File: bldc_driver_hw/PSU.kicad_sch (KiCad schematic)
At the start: 0 parts

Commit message: wip
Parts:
- added C1, C11, C16, C2, C3, C9: 100nF, Capacitor_SMD:C_0603_1608Metric_Pad1.08x0.95mm_HandSolder, symbol Device:C_Small
- added C10, C8: 47uF, Capacitor_SMD:C_0603_1608Metric_Pad1.08x0.95mm_HandSolder, symbol Device:C_Small
- added C12, C13, C14, C15, C4, C5: 10uF, Capacitor_SMD:C_0805_2012Metric_Pad1.18x1.45mm_HandSolder, symbol Device:C_Small
- added C6: 6.8nF, Capacitor_SMD:C_0603_1608Metric_Pad1.08x0.95mm_HandSolder, symbol Device:C_Small
- added C7: 6.8pF, Capacitor_SMD:C_0603_1608Metric_Pad1.08x0.95mm_HandSolder, symbol Device:C_Small
- added D1: 100V / 4A, Diode_SMD:D_SMB_Handsoldering, symbol Device:D_Schottky
- added L1: 68uH, symbol Device:L
- added R1: 140k, Resistor_SMD:R_0603_1608Metric_Pad0.98x0.95mm_HandSolder, symbol Device:R_Small
- added R2: 10k, Resistor_SMD:R_0603_1608Metric_Pad0.98x0.95mm_HandSolder, symbol Device:R_Small
- added R5: 100k, Resistor_SMD:R_0603_1608Metric_Pad0.98x0.95mm_HandSolder, symbol Device:R_Small
- added R6: 680k, Resistor_SMD:R_0603_1608Metric_Pad0.98x0.95mm_HandSolder, symbol Device:R_Small
- added U1: AMS1117-3.3, Package_TO_SOT_SMD:SOT-223-3_TabPin2, symbol Regulator_Linear:AMS1117-3.3
- added U2: TPS54260DGQ, Package_SO:MSOP-10-1EP_3x3mm_P0.5mm_EP2.2x3.1mm_Mask1.83x1.89mm_ThermalVias, symbol Regulator_Switching:TPS54260DGQ
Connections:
- new net: C7.1, R5.1, U2.8 (COMP)
- new net: R1.2, R2.1, U2.7 (VSENSE)
- new net: C1.2, D1.1 (K), L1.1, U2.1 (BOOT)
- new net: C1.1, U2.10 (PH)
- new net: C6.1, U2.4 (SS/TR)
- new net: R6.1, U2.5 (RT/CLK)
- new net: C3.1, R5.2
- new net +3.3V: C11.1, C14.1, C15.1, U1.2 (VO)
- new net +48V: C2.1, C4.1, C5.1, U2.2 (VIN)
- new net +5V: C12.1, C13.1, C16.1, U1.3 (VI)
- new net GND: C10.2, C11.2, C12.2, C13.2, C14.2, C15.2, C16.2, C2.2, C3.2, C4.2, C5.2, C6.2, C7.2, C8.2, C9.2, D1.2 (A), R2.2, R6.2, U1.1 (GND), U2.11 (GND), U2.9 (GND)
- new net Vdrive: C10.1, C8.1, C9.1, L1.2, R1.1
- no-connect marks 0 -> 2

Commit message: wip
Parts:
- added D7, D8: SS24, Diode_SMD:D_SMA, symbol Diode:SS24
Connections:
- net +5V: now also D7.1 (K), D8.1 (K)
- new net +5VD: D8.2 (A)
- new net VBUS: D7.2 (A)
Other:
- note added: "12V Aktualnie"
- moved on the sheet: C11, C12, C13, C14, C15, C16, R1, R2, U1

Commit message: wip
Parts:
- added D10: SS24, Diode_SMD:D_SMA, symbol Diode:SS24
- added NMT: 100k, Resistor_SMD:R_0603_1608Metric_Pad0.98x0.95mm_HandSolder, symbol Device:R_Small
- added R36: NMT, Resistor_SMD:R_0603_1608Metric_Pad0.98x0.95mm_HandSolder, symbol Device:R_Small
- L1: value 68uH -> 33uH; footprint (none) -> Inductor_SMD:L_Vishay_IHLP-4040
- R1: value 140k -> 52.3k
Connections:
- net Vdrive is gone; now on net +5V: C10.1, C8.1, C9.1, L1.2, R1.1
- net +48V: now also R36.1
- net +5V: now also D10.1 (K)
- net GND: now also NMT.2
- net at U2.3 (EN): now also NMT.1, R36.2
- new net VBUS2: D10.2 (A)
- no-connect marks 2 -> 1
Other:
- note removed: "12V Aktualnie"
- moved on the sheet: C1, C10, C11, C12, C13, C14, C15, C16, C2, C3, C4, C5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

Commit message: schematic finished pcb in progress
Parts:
- added TP4, TP5, TP6, TP7, TP8, TP9: TestPoint, TestPoint:TestPoint_Pad_D2.0mm, symbol Connector:TestPoint
- R11: renamed from R36; footprint Resistor_SMD:R_0603_1608Metric_Pad0.98x0.95mm_HandSolder -> Resistor_SMD:R_0603_1608Metric
- renumbered C12 to C10, C16 to C11, C1 to C12, C14 to C13, C15 to C14, C11 to C15, C8 to C16, C10 to C17, C9 to C18, C4 to C3, C5 to C4, C2 to C5, C7 to C6, C3 to C7, C6 to C8, C13 to C9, D8 to D1, D7 to D2, D10 to D3, D1 to D4, NMT to NMT1, R5 to R12, R6 to R13, R1 to R14, R2 to R15, U2 to U3, U1 to U4
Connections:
- net +3.3V: now also TP9.1
- net +5V: now also TP7.1; no longer C16.1, C17.1, C18.1, L1.2, R14.1
- net +5VD: now also C16.1, C17.1, C18.1, L1.2, R14.1, TP4.1
- net VBUS: now also TP5.1
- net VBUS2: now also TP6.1
- net +48V renamed VDD
- net VDD: now also TP8.1
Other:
- moved on the sheet: C13, C3, C4, C5, C6, C7, C8, NMT1, R11, R12, R13

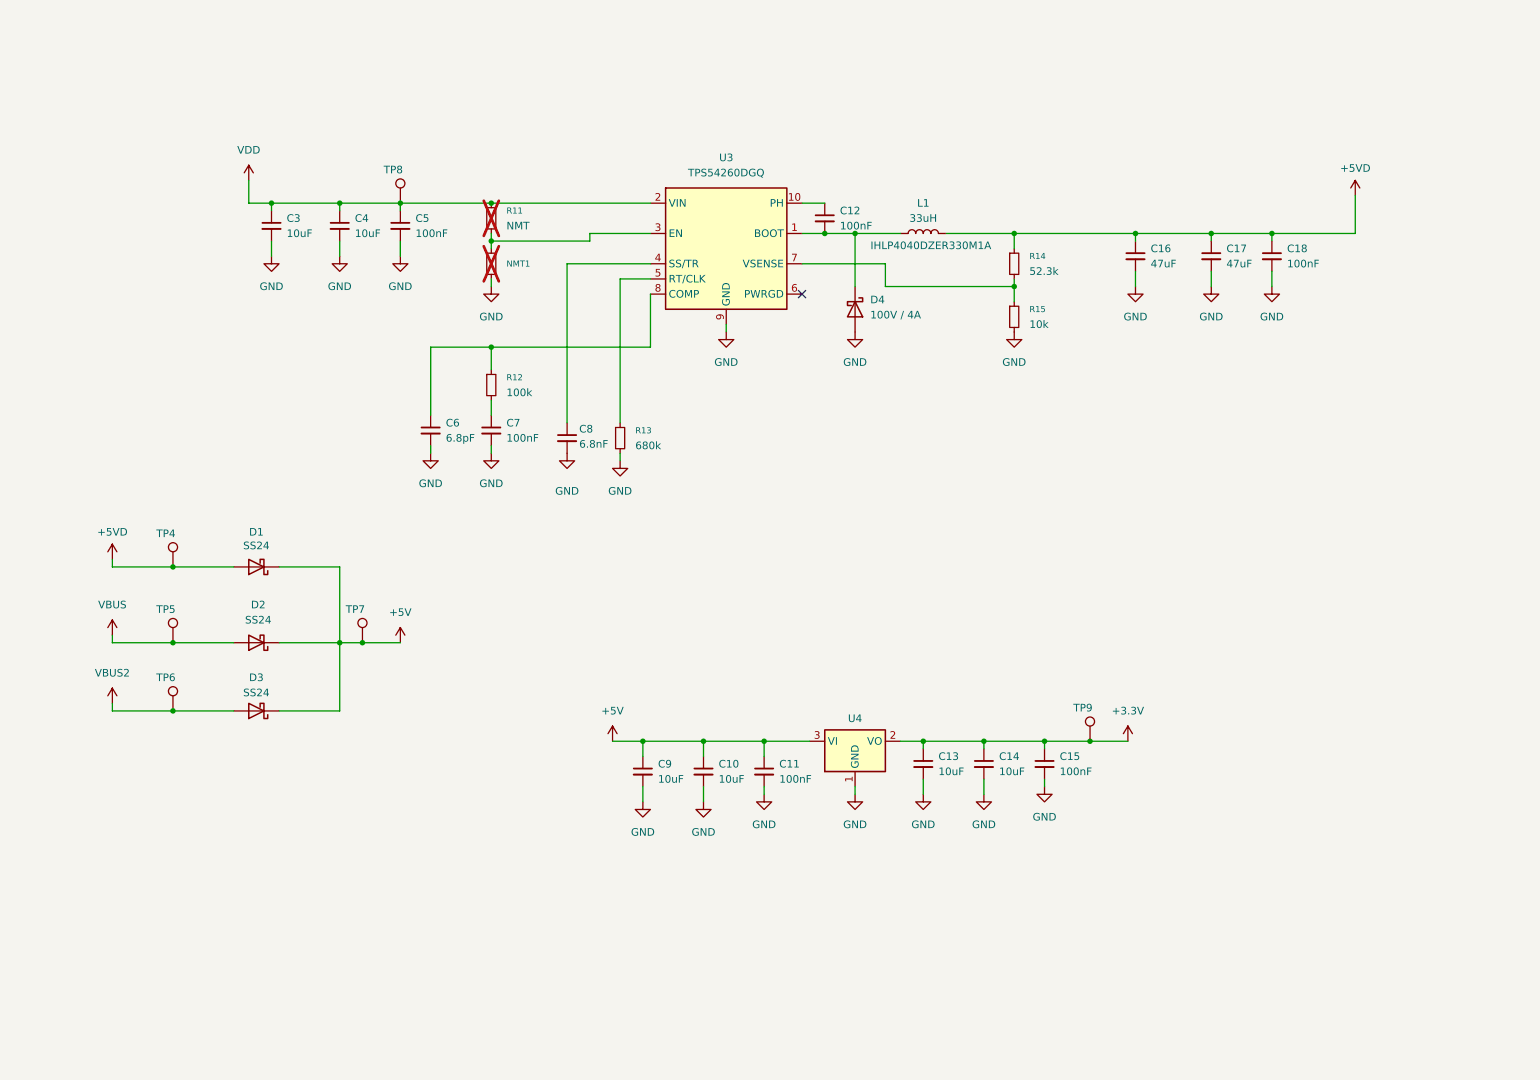
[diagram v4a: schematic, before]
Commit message: Changed one 3 phase driver to three h-bridges and changed buck converter which sink more current
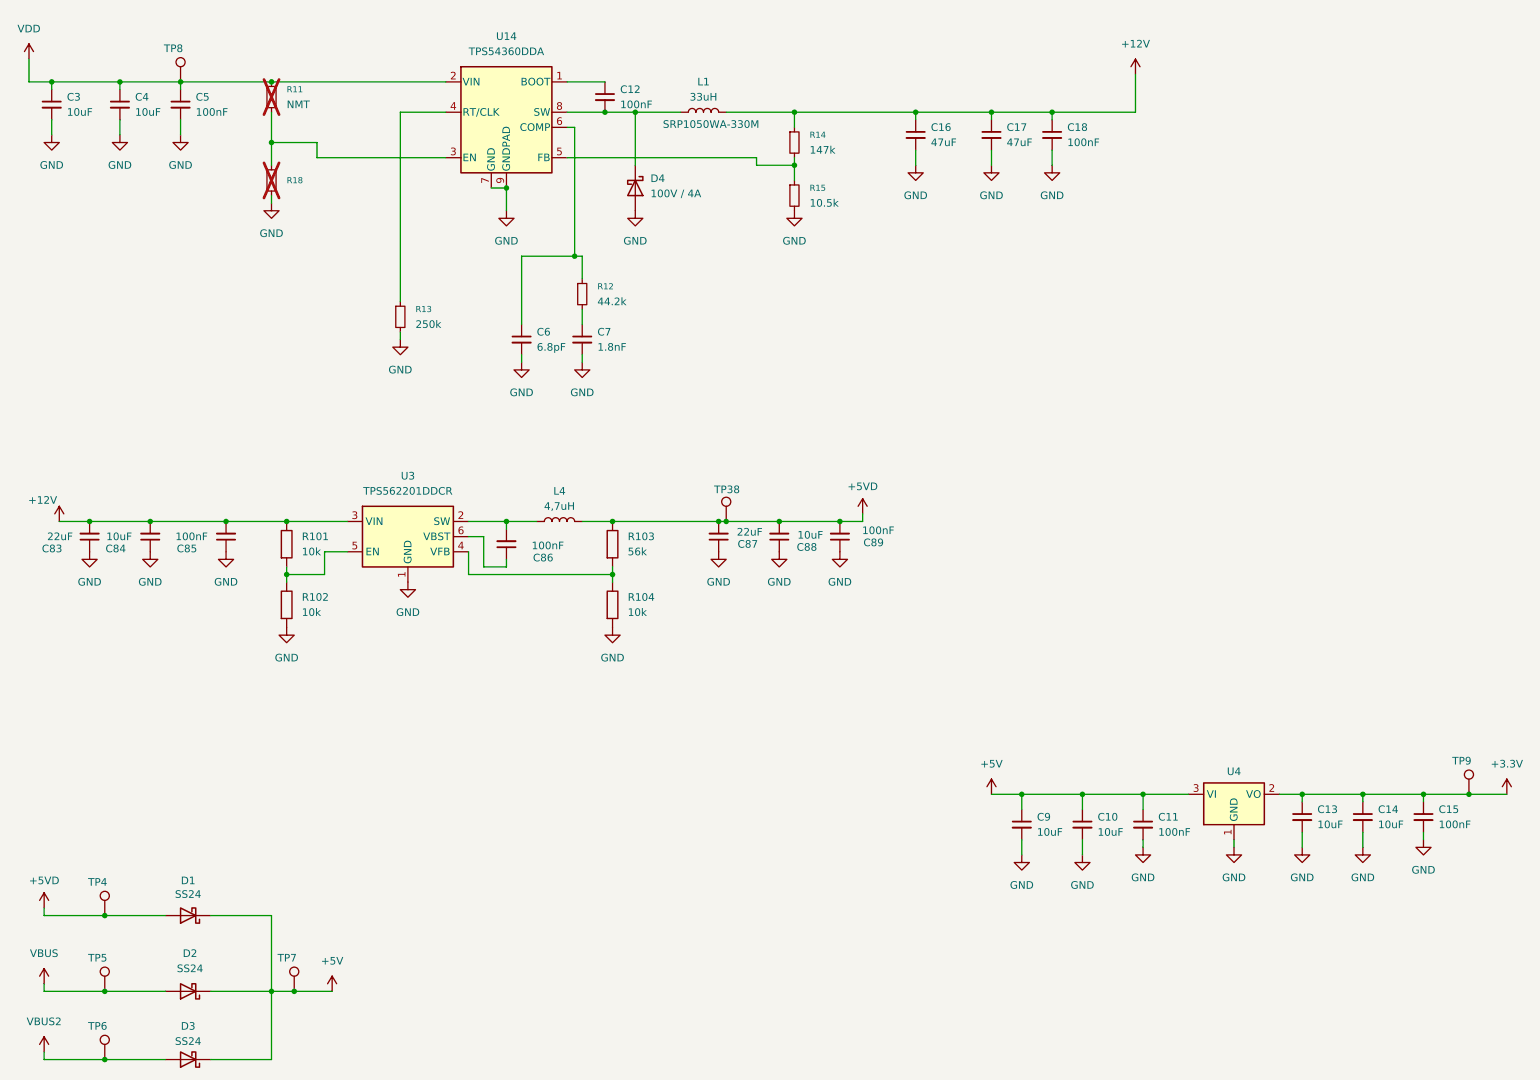
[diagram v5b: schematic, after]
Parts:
- removed C8: 6.8nF, Capacitor_SMD:C_0603_1608Metric_Pad1.08x0.95mm_HandSolder, symbol Device:C_Small
- removed U3: TPS54260DGQ, Package_SO:MSOP-10-1EP_3x3mm_P0.5mm_EP2.2x3.1mm_Mask1.83x1.89mm_ThermalVias, symbol Regulator_Switching:TPS54260DGQ
- added C83, C87: 22uF, Capacitor_SMD:C_0805_2012Metric_Pad1.18x1.45mm_HandSolder, symbol Device:C_Small
- added C84, C88: 10uF, Capacitor_SMD:C_0603_1608Metric_Pad1.08x0.95mm_HandSolder, symbol Device:C_Small
- added C85, C86, C89: 100nF, Capacitor_SMD:C_0603_1608Metric_Pad1.08x0.95mm_HandSolder, symbol Device:C_Small
- added L4: 4,7uH, bldc_driver_footprint:INDPM5452X300N, symbol Device:L
- added R101, R102, R104: 10k, Resistor_SMD:R_0603_1608Metric_Pad0.98x0.95mm_HandSolder, symbol PCM_SL_Resistors:Resistor
- added R103: 56k, Resistor_SMD:R_0603_1608Metric_Pad0.98x0.95mm_HandSolder, symbol PCM_SL_Resistors:Resistor
- added TP38: TestPoint, TestPoint:TestPoint_Pad_D2.0mm, symbol Connector:TestPoint
- added U14: TPS54360DDA, Package_SO:TI_SO-PowerPAD-8_ThermalVias, symbol Regulator_Switching:TPS54360DDA
- added U3: TPS562201DDCR, Package_TO_SOT_SMD:SOT-23-6_Handsoldering, symbol Regulator_Switching:TPS562200
- C7: value 100nF -> 1.8nF
- L1: footprint Inductor_SMD:L_Vishay_IHLP-4040 -> Inductor_SMD:L_Bourns_SRP1050WA
- R12: value 100k -> 44.2k
- R13: value 680k -> 250k
- R14: value 52.3k -> 147k; footprint Resistor_SMD:R_0603_1608Metric_Pad0.98x0.95mm_HandSolder -> Resistor_SMD:R_0603_1608Metric
- R15: value 10k -> 10.5k; footprint Resistor_SMD:R_0603_1608Metric_Pad0.98x0.95mm_HandSolder -> Resistor_SMD:R_0603_1608Metric
- R18: renamed from NMT1; footprint Resistor_SMD:R_0603_1608Metric_Pad0.98x0.95mm_HandSolder -> Resistor_SMD:R_0603_1608Metric
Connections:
- net +5VD: now also C87.2, C88.2, C89.2, L4.2, R103.2, TP38.1; no longer C16.1, C17.1, C18.1, L1.2, R14.1
- net GND: now also C83.1, C84.1, C85.1, C87.1, C88.1, C89.1, R102.1, R104.1, U14.7 (GND), U14.9 (GNDPAD), U3.1 (GND)
- net VDD: now also U14.2 (VIN)
- net at C6.1, R12.1: now also U14.6 (COMP)
- net at R14.2, R15.1: now also U14.5 (FB)
- net at C12.2, D4.1 (K), L1.1: now also U14.8 (SW)
- net at C12.1: now also U14.1 (BOOT)
- net at R11.2, R18.1: now also U14.3 (EN)
- net at R13.1: now also U14.4 (RT/CLK)
- new net: R103.1, R104.2, U3.4 (VFB)
- new net: R101.1, R102.2, U3.5 (EN)
- new net: C86.2, L4.1, U3.2 (SW)
- new net: C86.1, U3.6 (VBST)
- new net +12V: C16.1, C17.1, C18.1, C83.2, C84.2, C85.2, L1.2, R101.2, R14.1, U3.3 (VIN)
- no-connect marks 1 -> 0
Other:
- moved on the sheet: C10, C11, C12, C13, C14, C15, C16, C17, C18, C3, C4, C5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

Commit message: Board finished to review
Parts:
- removed TP4: TestPoint, TestPoint:TestPoint_Pad_D2.0mm, symbol Connector:TestPoint
- added TP15: TestPoint, TestPoint:TestPoint_Pad_D2.0mm, symbol Connector:TestPoint
- C10, C13, C14, C9: footprint Capacitor_SMD:C_0805_2012Metric_Pad1.18x1.45mm_HandSolder -> Capacitor_SMD:C_0603_1608Metric
- C11, C12, C15, C16, C17, C18, C5, C6, C7, C84, C85, C86, C88, C89: footprint Capacitor_SMD:C_0603_1608Metric_Pad1.08x0.95mm_HandSolder -> Capacitor_SMD:C_0603_1608Metric
- C3, C4, C83, C87: footprint Capacitor_SMD:C_0805_2012Metric_Pad1.18x1.45mm_HandSolder -> Capacitor_SMD:C_0805_2012Metric
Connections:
- net +12V: now also TP15.1

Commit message: wip
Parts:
- R101, R102, R103, R104, R12, R13: footprint Resistor_SMD:R_0603_1608Metric_Pad0.98x0.95mm_HandSolder -> Resistor_SMD:R_0603_1608Metric
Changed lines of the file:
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@@
 			)
 		)
-		(property "Footprint" "Resistor_SMD:R_0603_1608Metric_Pad0.98x0.95mm_HandSolder"
+		(property "Footprint" "Resistor_SMD:R_0603_1608Metric"
 			(at 81.28 66.04 0)
 			(effects
@@
 			)
 		)
-		(property "Footprint" "Resistor_SMD:R_0603_1608Metric_Pad0.98x0.95mm_HandSolder"
+		(property "Footprint" "Resistor_SMD:R_0603_1608Metric"
 			(at 121.158 113.411 0)
 			(effects
@@
 			)
 		)
-		(property "Footprint" "Resistor_SMD:R_0603_1608Metric_Pad0.98x0.95mm_HandSolder"
+		(property "Footprint" "Resistor_SMD:R_0603_1608Metric"
 			(at 66.548 113.411 0)
 			(effects
@@
 			)
 		)
-		(property "Footprint" "Resistor_SMD:R_0603_1608Metric_Pad0.98x0.95mm_HandSolder"
+		(property "Footprint" "Resistor_SMD:R_0603_1608Metric"
 			(at 111.76 62.23 0)
 			(effects
@@
 			)
 		)
-		(property "Footprint" "Resistor_SMD:R_0603_1608Metric_Pad0.98x0.95mm_HandSolder"
+		(property "Footprint" "Resistor_SMD:R_0603_1608Metric"
 			(at 121.158 103.251 0)
 			(effects
@@
 			)
 		)
-		(property "Footprint" "Resistor_SMD:R_0603_1608Metric_Pad0.98x0.95mm_HandSolder"
+		(property "Footprint" "Resistor_SMD:R_0603_1608Metric"
 			(at 66.548 103.251 0)
 			(effects

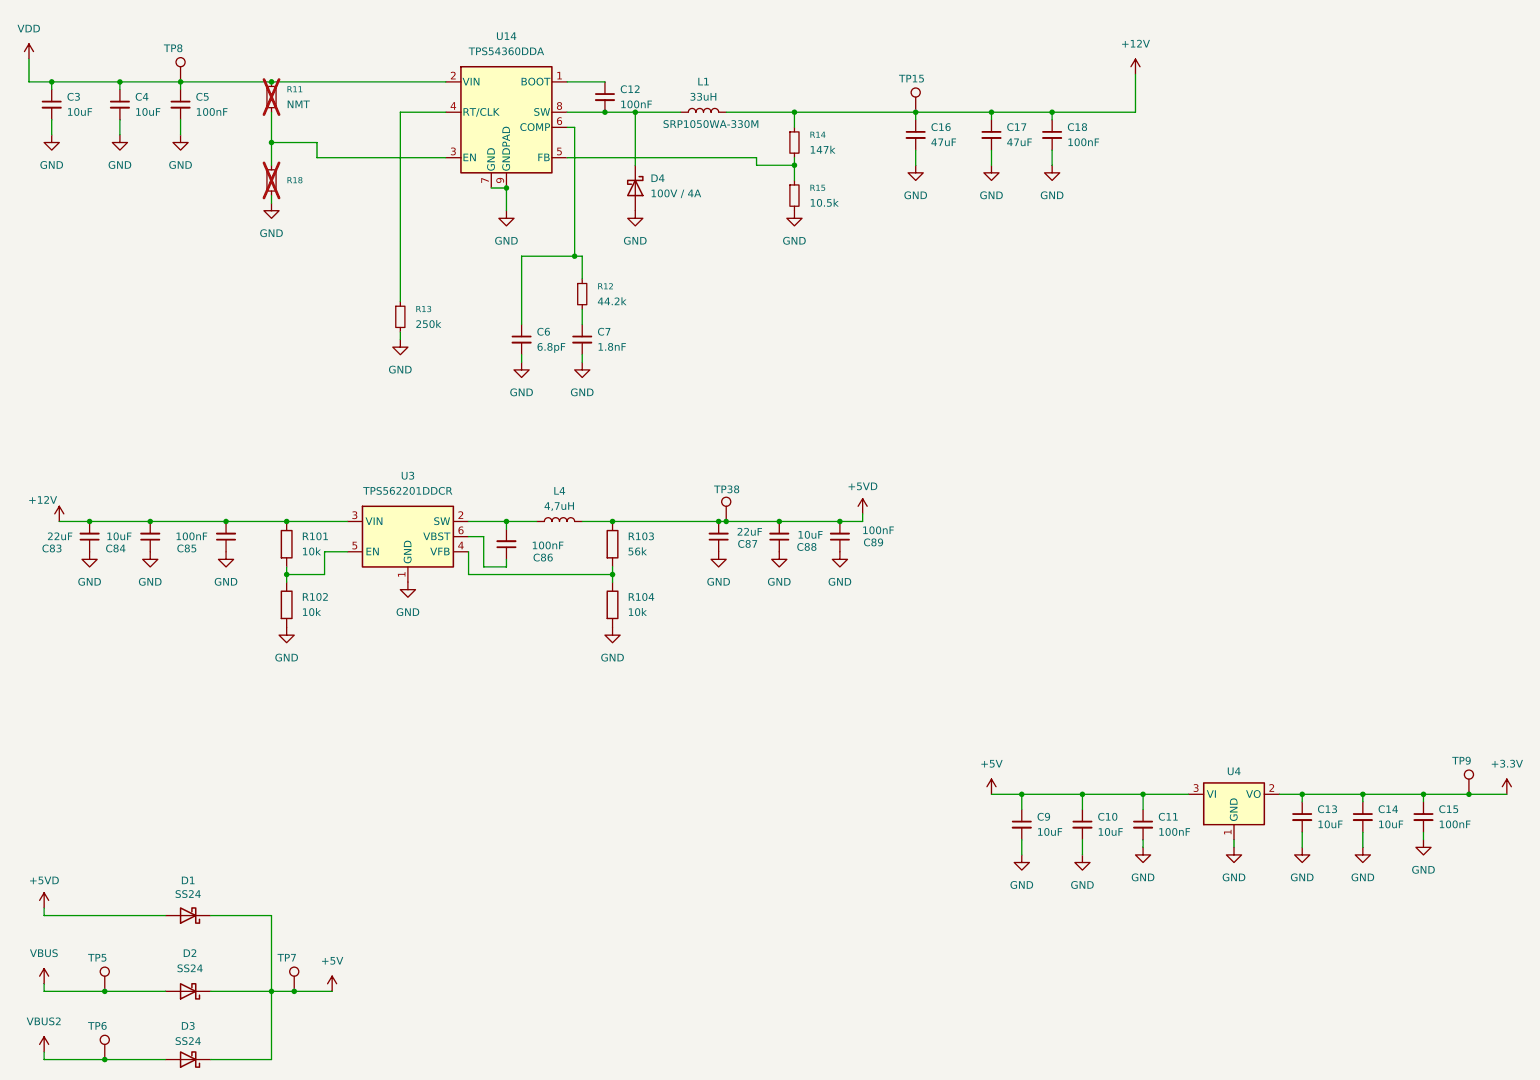
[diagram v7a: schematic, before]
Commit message: added lcsc codes
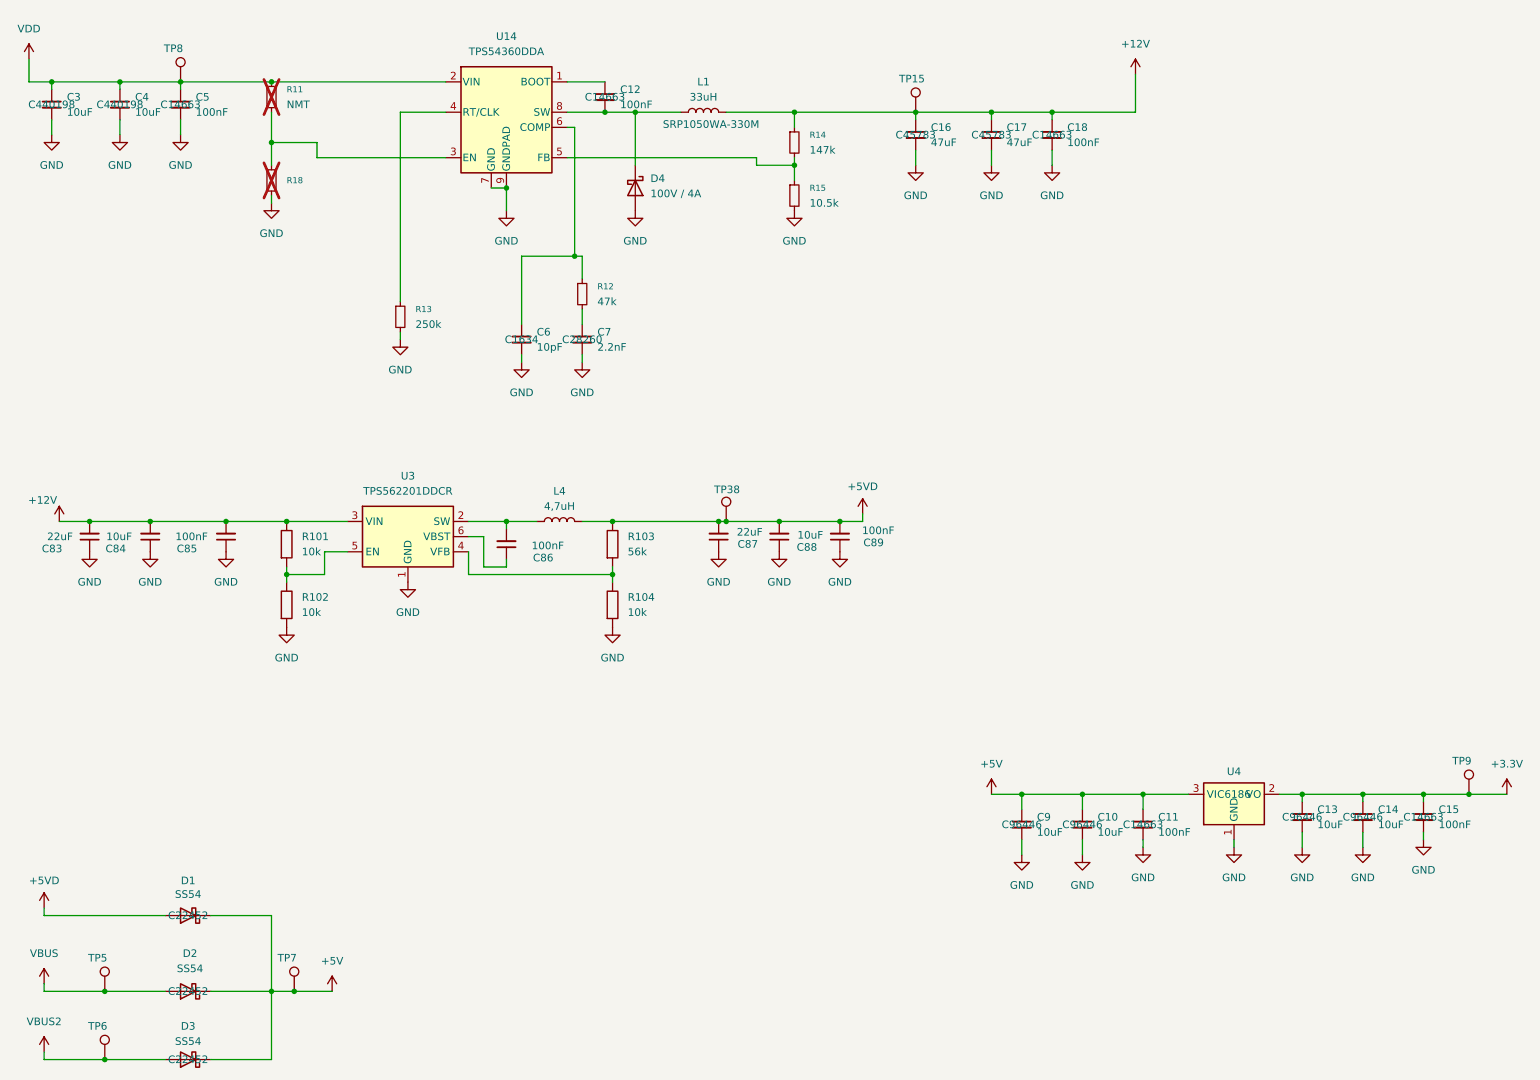
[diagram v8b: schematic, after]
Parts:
- C10, C13, C14, C9: LCSC (none) -> C96446
- C11, C12, C15, C18, C5: LCSC (none) -> C14663
- C16, C17: footprint Capacitor_SMD:C_0603_1608Metric -> Capacitor_SMD:C_0805_2012Metric; LCSC (none) -> C45783
- C3, C4: LCSC (none) -> C440198
- C6: value 6.8pF -> 10pF; LCSC (none) -> C1634
- C7: value 1.8nF -> 2.2nF; footprint Capacitor_SMD:C_0603_1608Metric -> Capacitor_SMD:C_0805_2012Metric; LCSC (none) -> C28260
- C83, C87: LCSC C96446 -> C45783
- C84, C88: LCSC C45783 -> C96446
- D1, D2, D3: value SS24 -> SS54; LCSC (none) -> C22452
- R12: value 44.2k -> 47k; LCSC (none) -> C25819
- U3: LCSC C90061 -> (none)
- U4: LCSC (none) -> C6186
